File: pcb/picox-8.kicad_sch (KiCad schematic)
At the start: 92 parts, among them J1 PX-8 Expansion Port, J2 Mini-DIN-8, J3 SD_Card, SW1 SW_Push, U1 XC95144XL-TQ100, U2 MAX3232, U3 Pico_W, U4 AZ1117-3.3

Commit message: pcb work
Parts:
- removed J3: SD_Card, Connector_Card:SD_TE_2041021, symbol Connector:SD_Card
- removed U4: AZ1117-3.3, Package_TO_SOT_SMD:SOT-223, symbol Regulator_Linear:AZ1117-3.3
- added C1, C2, C3, C4, C5, C6, C7: 100nF, Capacitor_SMD:C_0201_0603Metric_Pad0.64x0.40mm_HandSolder, symbol Device:C_Small
- added J3: 693063010911, hans-kicad-footprints:Wuerth SD Card 693063010911, symbol Wuerth SD Card 693063010911:693063010911
- added J4: USB_C_Receptacle_USB2.0, Connector_USB:USB_C_Receptacle_G-Switch_GT-USB-7010ASV, symbol Connector:USB_C_Receptacle_USB2.0
- added J5: CONN_CPLD_JTAG, Connector_IDC:IDC-Header_2x05_P2.54mm_Vertical, symbol Connector:Conn_ARM_JTAG_SWD_10
- added Q1: Q_PMOS_DGS, Package_TO_SOT_SMD:SOT-23-3, symbol Device:Q_PMOS_DGS
- added U5: MCP73871-2CC, Package_DFN_QFN:QFN-20-1EP_4x4mm_P0.5mm_EP2.5x2.5mm, symbol Battery_Management:MCP73871-2CC
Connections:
- net GND: now also SW1.2, U1.100 (GND), U1.21 (GND), U1.31 (GND), U1.44 (GND), U1.62 (GND), U1.69 (GND), U1.75 (GND), U1.84 (GND), U3.TP1 (USB_GND), C1.2, C2.2, C3.2, C4.2, C5.2, C6.2, C7.2, J3.3 (VSS1), J3.6 (VSS2), J3.S, J5.3 (GND), J5.5 (GND), J5.9 (GNDDetect)
- net BTN_FAILSAFE: now reaches SW1.1
- net BTN_FAILSAFE: now also U3.29 (GPIO22)
- net SD_MISO: now reaches U3.21 (GPIO16)
- net SD_MISO: now also J3.7 (DAT0)
- net SD_CS: now reaches U3.22 (GPIO17)
- net SD_CS: now also J3.1 (DAT3)
- net SD_CLK: now reaches U3.24 (GPIO18)
- net SD_CLK: now also J3.5 (CLK)
- net SD_MOSI: now reaches U3.25 (GPIO19)
- net SD_MOSI: now also J3.2 (CMD)
- net SD_CD: now reaches U3.26 (GPIO20)
- net SD_CD: now also J3.10 (CD)
- net SD_WP: now reaches U3.27 (GPIO21)
- net SD_WP: now also J3.11 (WP)
- net VSYS: now reaches U3.39 (VSYS)
- net VSYS: now also Q1.3 (S)
- net VBUS: now reaches U3.40 (VBUS)
- net VBUS: now also Q1.2 (G)
- net +3.3V: now reaches U1.26 (VCCIO)
- net +3.3V: now also U1.38 (VCCIO), U1.5 (VCCINT), U1.51 (VCCIO), U1.57 (VCCINT), U1.88 (VCCIO), U1.98 (VCCINT), C1.1, C2.1, C3.1, C4.1, C5.1, C6.1, C7.1, J3.4 (VDD), J5.1 (VTref)
- net at U1.45 (TDI): now also J5.8 (TDI)
- net at U1.47 (TMS): now also J5.2 (TMS)
- net at U1.48 (TCK): now also J5.4 (TCK)
- net at U1.83 (TDO): now also J5.6 (TDO)
- new net: Q1.1 (D), U5.1 (OUT), U5.20 (OUT)
- new net: U5.10 (V_{SS}), U5.11 (V_{SS}), U5.21 (V_{SS})
- new net: U5.14 (V_{BAT}), U5.15 (V_{BAT})
- new net: U5.18 (IN), U5.19 (IN)
- new net: J4.A1 (GND), J4.A12 (GND), J4.B1 (GND), J4.B12 (GND)
- new net: J4.A4 (VBUS), J4.A9 (VBUS), J4.B4 (VBUS), J4.B9 (VBUS)
- new net USB_D+: J4.A6 (D+), J4.B6 (D+), U3.TP3 (USB_D+)
- new net USB_D-: J4.A7 (D-), J4.B7 (D-), U3.TP2 (USB_D-)
- no-connect marks 0 -> 3
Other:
- moved on the sheet: J1, R1, R10, R11, R12, R13, R14, R15, R16, R17, R18, R19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

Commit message: cpld & pcb work
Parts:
- added C10, C11, C12, C8, C9: 100nF, Capacitor_SMD:C_0603_1608Metric_Pad1.08x0.95mm_HandSolder, symbol Device:C_Small
- added R85, R86: 10k, Resistor_SMD:R_0603_1608Metric_Pad0.98x0.95mm_HandSolder, symbol Device:R_Small
- added SW2: RESET, Button_Switch_THT:SW_Tactile_SPST_Angled_PTS645Vx39-2LFS, symbol Switch:SW_Push
- C1, C2, C3, C4, C5, C6, C7: footprint Capacitor_SMD:C_0201_0603Metric_Pad0.64x0.40mm_HandSolder -> Capacitor_SMD:C_0603_1608Metric_Pad1.08x0.95mm_HandSolder
- J2: value Mini-DIN-8 -> SERIAL
- SW1: value SW_Push -> FAILSAFE
- U2: value MAX3232 -> MAX3222; footprint Package_SO:SOP-16_3.9x9.9mm_P1.27mm -> Package_SO:TSSOP-20-1EP_4.4x6.5mm_P0.65mm_EP2.15x3.35mm
- U3: footprint RPI PIco:RPi_Pico_SMD_TH -> RPI PIco:RPI Pico W USB and Prog
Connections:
- net +3.3V: now also U2.19 (VCC), U3.35 (ADC_VREF), U3.36 (3V3), C12.1
- net BTN_FAILSAFE: now also U1.90 (P90); no longer U3.29 (GPIO22)
- net GND: now also J2.1, J2.10 (SHIELD), J2.11 (SHIELD), J2.9 (SHIELD), J4.A1 (GND), J4.A12 (GND), J4.B1 (GND), J4.B12 (GND), J4.S1 (SHIELD), U2.18 (GND), U3.13 (GND), U3.18 (GND), U3.23 (GND), U3.28 (GND), U3.3 (GND), U3.33 (AGND), U3.38 (GND), U3.8 (GND), C10.2, C11.2, C12.2, R86.2, SW2.2
- net SD_CD: now also U1.89 (P89); no longer U3.26 (GPIO20)
- net SD_WP: now also U1.87 (P87); no longer U3.27 (GPIO21)
- net SPI: now also R85.2, R86.1
- net VB1: now also Q1.1 (D), U5.1 (OUT), U5.20 (OUT)
- net VBUS: now also J4.A4 (VBUS), J4.A9 (VBUS), J4.B4 (VBUS), J4.B9 (VBUS), U5.2 (VPCC); no longer Q1.2 (G), U3.40 (VBUS)
- net at J2.2: now also U2.16 (R1IN)
- net at J2.3: now also U2.17 (T1OUT)
- net at J2.6: now also U2.8 (T2OUT)
- net at J2.7: now also U2.9 (R2IN)
- net PICO_TXD0: now reaches U3.1 (GPIO0)
- net PICO_TXD0: now also U1.33 (P33)
- net PICO_D5: now reaches U3.10 (GPIO7)
- net PICO_D5: now also U1.20 (P20)
- net PICO_D6: now reaches U3.11 (GPIO8)
- net PICO_D6: now also U1.19 (P19)
- net PICO_D7: now reaches U3.12 (GPIO9)
- net PICO_D7: now also U1.18 (P18)
- net PICO_CLK: now reaches U3.14 (GPIO10)
- net PICO_CLK: now also U1.17 (P17)
- net PICO_DIR: now reaches U3.15 (GPIO11)
- net PICO_DIR: now also U1.16 (P16)
- net PICO_STB: now reaches U3.16 (GPIO12)
- net PICO_STB: now also U1.15 (P15)
- net PICO_A0: now reaches U3.17 (GPIO13)
- net PICO_A0: now also U1.14 (P14)
- net PICO_A1: now reaches U3.19 (GPIO14)
- net PICO_A1: now also U1.13 (P13)
- net PICO_RXD0: now reaches U3.2 (GPIO1)
- net PICO_RXD0: now also U1.32 (P32)
- net PICO_A2: now reaches U3.20 (GPIO15)
- net PICO_A2: now also U1.12 (P12)
- net PICO_RUN: now reaches U3.30 (RUN)
- net PICO_SER_HSOUT: now reaches U3.31 (GPIO26_ADC0)
- net PICO_SER_HSIN: now reaches U3.32 (GPIO27_ADC1)
- net at U3.34 (GPIO28_ADC2): now also R85.1
- net PICO_D0: now reaches U3.4 (GPIO2)
- net PICO_D0: now also U1.30 (P30)
- net PICO_D1: now reaches U3.5 (GPIO3)
- net PICO_D1: now also U1.29 (P29)
- net PICO_D2: now reaches U3.6 (GPIO4)
- net PICO_D2: now also U1.28 (P28)
- net PICO_D3: now reaches U3.7 (GPIO5)
- net PICO_D3: now also U1.25 (P25)
- net PICO_D4: now reaches U3.9 (GPIO6)
- net PICO_D4: now also U1.24 (P24)
- net ~{SER_EN}: now reaches U2.1 (~{EN})
- net ~{SER_EN}: now also U1.8 (P8)
- net SER_HSIN: now reaches U2.10 (R2OUT)
- net SER_HSIN: now also U1.11 (P11)
- net SER_HSOUT: now reaches U2.12 (T2IN)
- net SER_HSOUT: now also U1.10 (P10)
- net PICO_TXD1: now reaches U2.13 (T1IN)
- net PICO_TXD1: now also U3.26 (GPIO20)
- net PICO_RXD1: now reaches U2.15 (R1OUT)
- net PICO_RXD1: now also U3.27 (GPIO21)
- net at U2.2 (C1+): now also C8.1
- net at U2.3 (VS+): now also C10.1
- net at U2.4 (C1-): now also C8.2
- net at U2.5 (C2+): now also C9.1
- net at U2.6 (C2-): now also C9.2
- net at U2.7 (VS-): now also C11.1
- net ~{SER_SHDN}: now reaches U1.9 (P9)
- net ~{SER_SHDN}: now also U2.20 (~{SHDN})
- net BTN_RESET: now reaches U1.91 (P91)
- net BTN_RESET: now also SW2.1
- net PICO_RESET: now reaches U1.92 (P92)
- net PICO_BOOTSEL: now reaches U1.93 (P93)
- net PICO_BOOTSEL: now also U3.TP6 (BOOTSEL)
- net VSYS renamed PICO_VSYS
- new net PICO_VBUS: Q1.2 (G), U3.40 (VBUS)
- no-connect marks 3 -> 7
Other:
- moved on the sheet: J2

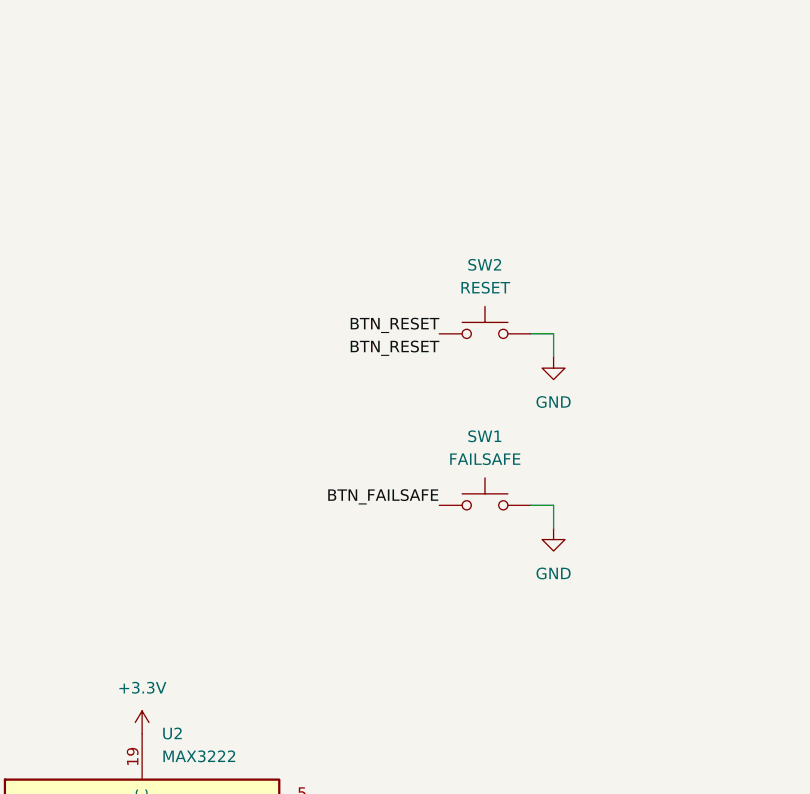
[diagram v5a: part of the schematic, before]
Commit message: schematics work: buttons hooked up
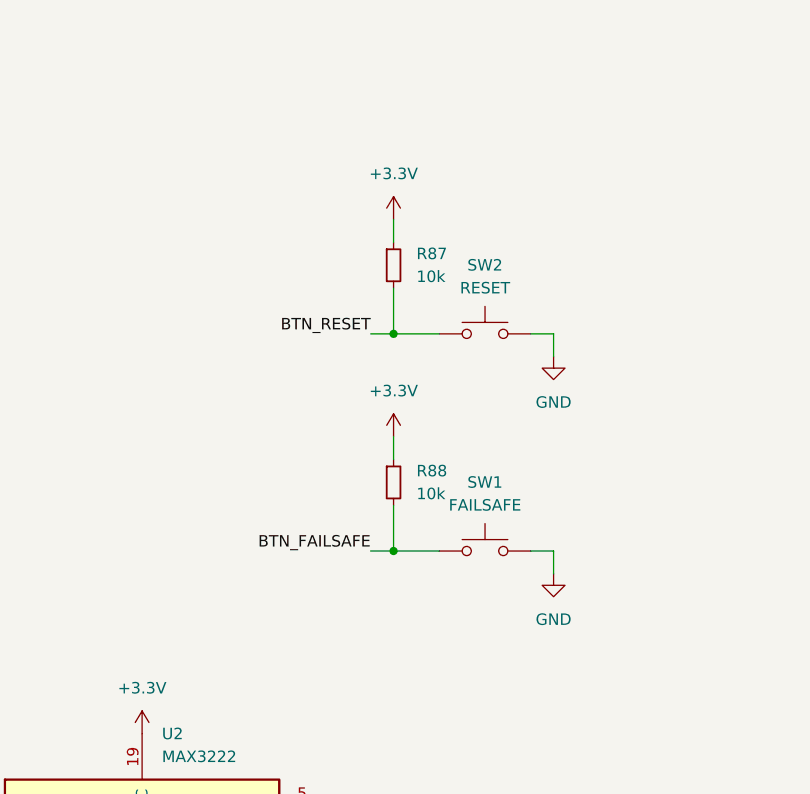
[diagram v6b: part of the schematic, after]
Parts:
- added R87, R88: 10k, Resistor_SMD:R_0603_1608Metric_Pad0.98x0.95mm_HandSolder, symbol Device:R_Small
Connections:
- net +3.3V: now also R87.1, R88.1
- net BTN_FAILSAFE: now also R88.2
- net BTN_RESET: now also R87.2
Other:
- moved on the sheet: SW1
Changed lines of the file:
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@@
   (junction (at 247.65 332.74) (diameter 0) (color 0 0 0 0)
   )
+  (junction (at 447.04 255.27) (diameter 0) (color 0 0 0 0)
+  )
   (junction (at 293.37 322.58) (diameter 0) (color 0 0 0 0)
   )
@@
   (junction (at 281.94 332.74) (diameter 0) (color 0 0 0 0)
   )
+  (junction (at 447.04 231.14) (diameter 0) (color 0 0 0 0)
+  )
   (junction (at 171.45 29.21) (diameter 0) (color 0 0 0 0)
   )
@@
     (stroke (width 0) (type default))
   )
+  (wire (pts (xy 444.5 255.27) (xy 447.04 255.27))
+    (stroke (width 0) (type default))
+  )
   (wire (pts (xy 496.57 81.28) (xy 499.11 81.28))
     (stroke (width 0) (type default))
@@
     (stroke (width 0) (type default))
   )
+  (wire (pts (xy 444.5 231.14) (xy 447.04 231.14))
+    (stroke (width 0) (type default))
+  )
   (wire (pts (xy 259.08 322.58) (xy 259.08 325.12))
     (stroke (width 0) (type default))
@@
     (stroke (width 0) (type default))
   )
-  (wire (pts (xy 464.82 250.19) (xy 464.82 252.73))
+  (wire (pts (xy 464.82 255.27) (xy 464.82 257.81))
     (stroke (width 0) (type default))
   )
@@
     (stroke (width 0) (type default))
   )
+  (wire (pts (xy 447.04 226.06) (xy 447.04 231.14))
+    (stroke (width 0) (type default))
+  )
   (wire (pts (xy 336.55 88.9) (xy 336.55 91.44))
     (stroke (width 0) (type default))
@@
     (stroke (width 0) (type default))
   )
+  (wire (pts (xy 447.04 242.57) (xy 447.04 245.11))
+    (stroke (width 0) (type default))
+  )
   (wire (pts (xy 316.23 33.02) (xy 320.04 33.02))
     (stroke (width 0) (type default))
@@
     (stroke (width 0) (type default))
   )
+  (wire (pts (xy 447.04 250.19) (xy 447.04 255.27))
+    (stroke (width 0) (type default))
+  )
   (wire (pts (xy 421.64 81.28) (xy 421.64 83.82))
     (stroke (width 0) (type default))
@@
     (stroke (width 0) (type default))
   )
+  (wire (pts (xy 447.04 255.27) (xy 452.12 255.27))
+    (stroke (width 0) (type default))
+  )
   (wire (pts (xy 341.63 254) (xy 341.63 265.43))
     (stroke (width 0) (type default))
@@
     (stroke (width 0) (type default))
   )
+  (wire (pts (xy 447.04 231.14) (xy 452.12 231.14))
+    (stroke (width 0) (type default))
+  )
   (wire (pts (xy 541.02 91.44) (xy 549.91 91.44))
     (stroke (width 0) (type default))
@@
     (stroke (width 0) (type default))
   )
+  (wire (pts (xy 447.04 218.44) (xy 447.04 220.98))
+    (stroke (width 0) (type default))
+  )
   (wire (pts (xy 384.81 214.63) (xy 394.97 214.63))
     (stroke (width 0) (type default))
@@
     (stroke (width 0) (type default))
   )
-  (wire (pts (xy 462.28 250.19) (xy 464.82 250.19))
+  (wire (pts (xy 462.28 255.27) (xy 464.82 255.27))
     (stroke (width 0) (type default))
   )
@@
     (effects (font (size 1.27 1.27)) (justify right bottom))
   )
-  (label "BTN_RESET" (at 452.12 233.68 180) (fields_autoplaced)
-    (effects (font (size 1.27 1.27)) (justify right bottom))
-  )
   (label "~{TXD}" (at 398.78 129.54 0) (fields_autoplaced)
     (effects (font (size 1.27 1.27)) (justify left bottom))
@@
     (effects (font (size 1.27 1.27)) (justify left bottom))
   )
-  (label "BTN_RESET" (at 452.12 231.14 180) (fields_autoplaced)
+  (label "BTN_RESET" (at 444.5 231.14 180) (fields_autoplaced)
     (effects (font (size 1.27 1.27)) (justify right bottom))
   )
@@
     (effects (font (size 1.27 1.27)) (justify right bottom))
   )
-  (label "BTN_FAILSAFE" (at 452.12 250.19 180) (fields_autoplaced)
+  (label "BTN_FAILSAFE" (at 444.5 255.27 180) (fields_autoplaced)
     (effects (font (size 1.27 1.27)) (justify right bottom))
   )
@@
     )
   )
-  (symbol (lib_id "power:GND") (at 464.82 252.73 0) (unit 1)
+  (symbol (lib_id "power:GND") (at 464.82 257.81 0) (unit 1)
     (in_bom yes) (on_board yes) (dnp no) (fields_autoplaced)
-    (property "Reference" "#PWR052" (at 464.82 259.08 0)
+    (property "Reference" "#PWR052" (at 464.82 264.16 0)
       (effects (font (size 1.27 1.27)) hide)
     )
-    (property "Value" "GND" (at 464.82 257.81 0)
+    (property "Value" "GND" (at 464.82 262.89 0)
       (effects (font (size 1.27 1.27)))
     )
-    (property "Footprint" "" (at 464.82 252.73 0)
+    (property "Footprint" "" (at 464.82 257.81 0)
       (effects (font (size 1.27 1.27)) hide)
     )
-    (property "Datasheet" "" (at 464.82 252.73 0)
+    (property "Datasheet" "" (at 464.82 257.81 0)
       (effects (font (size 1.27 1.27)) hide)
     )
@@
     )
   )
-  (symbol (lib_id "Switch:SW_Push") (at 457.2 250.19 0) (unit 1)
+  (symbol (lib_id "Switch:SW_Push") (at 457.2 255.27 0) (unit 1)
     (in_bom yes) (on_board yes) (dnp no)
-    (property "Reference" "SW1" (at 457.2 242.57 0)
+    (property "Reference" "SW1" (at 457.2 247.65 0)
       (effects (font (size 1.27 1.27)))
     )
-    (property "Value" "FAILSAFE" (at 457.2 245.11 0)
+    (property "Value" "FAILSAFE" (at 457.2 250.19 0)
       (effects (font (size 1.27 1.27)))
     )
-    (property "Footprint" "Button_Switch_THT:SW_Tactile_SPST_Angled_PTS645Vx39-2LFS" (at 457.2 245.11 0)
+    (property "Footprint" "Button_Switch_THT:SW_Tactile_SPST_Angled_PTS645Vx39-2LFS" (at 457.2 250.19 0)
       (effects (font (size 1.27 1.27)) hide)
     )
-    (property "Datasheet" "~" (at 457.2 245.11 0)
+    (property "Datasheet" "~" (at 457.2 250.19 0)
       (effects (font (size 1.27 1.27)) hide)
     )
@@
     )
   )
+  (symbol (lib_id "power:+3.3V") (at 447.04 242.57 0) (unit 1)
+    (in_bom yes) (on_board yes) (dnp no) (fields_autoplaced)
+    (property "Reference" "#PWR062" (at 447.04 246.38 0)
+      (effects (font (size 1.27 1.27)) hide)
+    )
+    (property "Value" "+3.3V" (at 447.04 237.49 0)
+      (effects (font (size 1.27 1.27)))
+    )
+    (property "Footprint" "" (at 447.04 242.57 0)
+      (effects (font (size 1.27 1.27)) hide)
+    )
+    (property "Datasheet" "" (at 447.04 242.57 0)
+      (effects (font (size 1.27 1.27)) hide)
+    )
+    (pin "1")
+    (instances
+      (project "picox-8"
+        (path "/b3edc386-2a93-4110-82fb-ef41abb72a44"
+          (reference "#PWR062") (unit 1)
+        )
+      )
+    )
+  )
   (symbol (lib_id "power:GND") (at 397.51 91.44 0) (unit 1)
     (in_bom yes) (on_board yes) (dnp no) (fields_autoplaced)
@@
     )
   )
+  (symbol (lib_id "Device:R_Small") (at 447.04 223.52 0) (unit 1)
+    (in_bom yes) (on_board yes) (dnp no) (fields_autoplaced)
+    (property "Reference" "R87" (at 449.58 222.25 0)
+      (effects (font (size 1.27 1.27)) (justify left))
+    )
+    (property "Value" "10k" (at 449.58 224.79 0)
+      (effects (font (size 1.27 1.27)) (justify left))
+    )
+    (property "Footprint" "Resistor_SMD:R_0603_1608Metric_Pad0.98x0.95mm_HandSolder" (at 447.04 223.52 0)
+      (effects (font (size 1.27 1.27)) hide)
+    )
+    (property "Datasheet" "~" (at 447.04 223.52 0)
+      (effects (font (size 1.27 1.27)) hide)
+    )
+    (pin "1")
+    (pin "2")
+    (instances
+      (project "picox-8"
+        (path "/b3edc386-2a93-4110-82fb-ef41abb72a44"
+          (reference "R87") (unit 1)
+        )
+      )
+    )
+  )
   (symbol (lib_id "power:GND") (at 336.55 91.44 0) (unit 1)
     (in_bom yes) (on_board yes) (dnp no) (fields_autoplaced)
@@
     )
   )
+  (symbol (lib_id "Device:R_Small") (at 447.04 247.65 0) (unit 1)
+    (in_bom yes) (on_board yes) (dnp no) (fields_autoplaced)
+    (property "Reference" "R88" (at 449.58 246.38 0)
+      (effects (font (size 1.27 1.27)) (justify left))
+    )
+    (property "Value" "10k" (at 449.58 248.92 0)
+      (effects (font (size 1.27 1.27)) (justify left))
+    )
+    (property "Footprint" "Resistor_SMD:R_0603_1608Metric_Pad0.98x0.95mm_HandSolder" (at 447.04 247.65 0)
+      (effects (font (size 1.27 1.27)) hide)
+    )
+    (property "Datasheet" "~" (at 447.04 247.65 0)
+      (effects (font (size 1.27 1.27)) hide)
+    )
+    (pin "1")
+    (pin "2")
+    (instances
+      (project "picox-8"
+        (path "/b3edc386-2a93-4110-82fb-ef41abb72a44"
+          (reference "R88") (unit 1)
+        )
+      )
+    )
+  )
   (symbol (lib_id "power:+3.3V") (at 247.65 320.04 0) (unit 1)
     (in_bom yes) (on_board yes) (dnp no) (fields_autoplaced)
@@
         )
       )
+    )
+  )
+  (symbol (lib_id "power:+3.3V") (at 447.04 218.44 0) (unit 1)
+    (in_bom yes) (on_board yes) (dnp no) (fields_autoplaced)
+    (property "Reference" "#PWR061" (at 447.04 222.25 0)
+      (effects (font (size 1.27 1.27)) hide)
+    )
+    (property "Value" "+3.3V" (at 447.04 213.36 0)
+      (effects (font (size 1.27 1.27)))
+    )
+    (property "Footprint" "" (at 447.04 218.44 0)
+      (effects (font (size 1.27 1.27)) hide)
+    )
+    (property "Datasheet" "" (at 447.04 218.44 0)
+      (effects (font (size 1.27 1.27)) hide)
+    )
+    (pin "1")
+    (instances
+      (project "picox-8"
+        (path "/b3edc386-2a93-4110-82fb-ef41abb72a44"
+          (reference "#PWR061") (unit 1)
+        )
+      )

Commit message: schematic nearing completion
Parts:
- added C13: 10μF, Capacitor_SMD:C_0603_1608Metric_Pad1.08x0.95mm_HandSolder, symbol Device:C_Small
- added C14, C15: 4.7μF, Capacitor_SMD:C_0603_1608Metric_Pad1.08x0.95mm_HandSolder, symbol Device:C_Small
- added D1: LED0, LED_SMD:LED_0603_1608Metric_Pad1.05x0.95mm_HandSolder, symbol Device:LED_Small
- added D2: LED1, LED_SMD:LED_0603_1608Metric_Pad1.05x0.95mm_HandSolder, symbol Device:LED_Small
- added D3: LED2, LED_SMD:LED_0603_1608Metric_Pad1.05x0.95mm_HandSolder, symbol Device:LED_Small
- added D4: LED3, LED_SMD:LED_0603_1608Metric_Pad1.05x0.95mm_HandSolder, symbol Device:LED_Small
- added J6: NTC, Connector_PinHeader_2.54mm:PinHeader_1x02_P2.54mm_Vertical, symbol Connector_Generic:Conn_01x02
- added J7: BAT, Connector_JST:JST_EH_S2B-EH_1x02_P2.50mm_Horizontal, symbol Connector_Generic:Conn_01x02
- added R89: 0, Resistor_SMD:R_0603_1608Metric_Pad0.98x0.95mm_HandSolder, symbol Device:R_Small
- added R90: DNP, Resistor_SMD:R_0603_1608Metric_Pad0.98x0.95mm_HandSolder, symbol Device:R_Small
- added R91, R94: 1k, Resistor_SMD:R_0603_1608Metric_Pad0.98x0.95mm_HandSolder, symbol Device:R_Small
- added R92, R93: 10k, Resistor_SMD:R_0603_1608Metric_Pad0.98x0.95mm_HandSolder, symbol Device:R_Small
- added R95, R96, R97, R98: 120, Resistor_SMD:R_0603_1608Metric_Pad0.98x0.95mm_HandSolder, symbol Device:R_Small
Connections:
- net +3.3V: now also D1.2 (A), D2.2 (A), D3.2 (A), D4.2 (A)
- net GND: now also U5.10 (V_{SS}), U5.11 (V_{SS}), U5.21 (V_{SS}), C13.2, C14.2, C15.2, J6.2 (Pin_2), J7.2 (Pin_2), R90.1, R91.2, R92.1, R93.1, R94.2
- net VB1: now also C14.1
- net VBUS: now also U5.18 (IN), U5.19 (IN), C13.1
- net at U5.12 (PROG3): now also R92.2
- net at U5.13 (PROG1): now also R91.1
- net VBAT: now reaches U5.14 (V_{BAT}), U5.15 (V_{BAT})
- net VBAT: now also U5.16 (V_{BAT_SENSE}), C15.1, J7.1 (Pin_1)
- net CHG_CE: now reaches U5.17 (CE)
- net CHG_CE: now also U1.2 (I/O/GTS4)
- net CHG_SEL: now reaches U5.3 (SEL)
- net CHG_SEL: now also U1.97 (P97)
- net CHG_PROG2: now reaches U5.4 (PROG2)
- net CHG_PROG2: now also U1.99 (I/O/GSR)
- net at U5.5 (THERM): now also R89.1
- net CHG_~{PG}: now reaches U5.6 (~{PG})
- net CHG_~{PG}: now also U1.96 (P96)
- net CHG_STAT2: now reaches U5.7 (STAT2)
- net CHG_STAT2: now also U1.95 (P95)
- net CHG_STAT1: now reaches U5.8 (STAT1/~{LBO})
- net CHG_STAT1: now also U1.94 (P94)
- net CHG_~{TE}: now reaches U5.9 (~{TE})
- net CHG_~{TE}: now also U1.1 (I/O/GTS3)
- net at J4.A5 (CC1): now also R94.1
- net at J4.B5 (CC2): now also R93.2
- net LED0: now reaches U1.3 (I/O/GTS1)
- net LED0: now also R95.2
- net LED1: now reaches U1.4 (I/O/GTS2)
- net LED1: now also R96.2
- net LED2: now reaches U1.6 (P6)
- net LED2: now also R97.2
- net LED3: now reaches U1.7 (P7)
- net LED3: now also R98.2
- new net: D3.1 (K), R97.1
- new net: D4.1 (K), R98.1
- new net: D1.1 (K), R95.1
- new net: D2.1 (K), R96.1
- new net NTC: J6.1 (Pin_1), R89.2, R90.2
- no-connect marks 7 -> 9
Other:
- moved on the sheet: J3, Q1

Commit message: erc fixes
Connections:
- net CHG_CE: now also U1.3 (I/O/GTS1); no longer U1.2 (I/O/GTS4)
- net CHG_PROG2: now also U1.1 (I/O/GTS3); no longer U1.99 (I/O/GSR)
- net CHG_SEL: now also U1.99 (I/O/GSR); no longer U1.97 (P97)
- net CHG_STAT1: now also U1.95 (P95); no longer U1.94 (P94)
- net CHG_STAT2: now also U1.96 (P96); no longer U1.95 (P95)
- net CHG_~{PG}: now also U1.97 (P97); no longer U1.96 (P96)
- net CHG_~{TE}: now also U1.2 (I/O/GTS4); no longer U1.1 (I/O/GTS3)
- net LED0: now also U1.4 (I/O/GTS2); no longer U1.3 (I/O/GTS1)
- net LED1: now also U1.6 (P6); no longer U1.4 (I/O/GTS2)
- net LED2: now also U1.7 (P7); no longer U1.6 (P6)
- net LED3: now also U1.8 (P8); no longer U1.7 (P7)
- net PICO_RUN: now also U1.94 (P94)
- net PICO_SER_HSIN: now also U2.10 (R2OUT)
- net PICO_SER_HSOUT: now also U2.12 (T2IN)
- net ~{SER_EN}: now also U1.9 (P9); no longer U1.8 (P8)
- net ~{SER_SHDN}: now also U1.10 (P10); no longer U1.9 (P9)
- net PICO_RESET: no longer names the net of U1.92 (P92)
- net SER_HSIN: no longer names the net of U1.11 (P11)
- net SER_HSIN: no longer U2.10 (R2OUT)
- removed net SER_HSOUT: U1.10 (P10), U2.12 (T2IN)
- no-connect marks 9 -> 16
